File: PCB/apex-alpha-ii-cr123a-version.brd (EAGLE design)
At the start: 13.1 x 74.7 mm, 31 parts, among them IC1 CC430F5135, Y1 26MHz

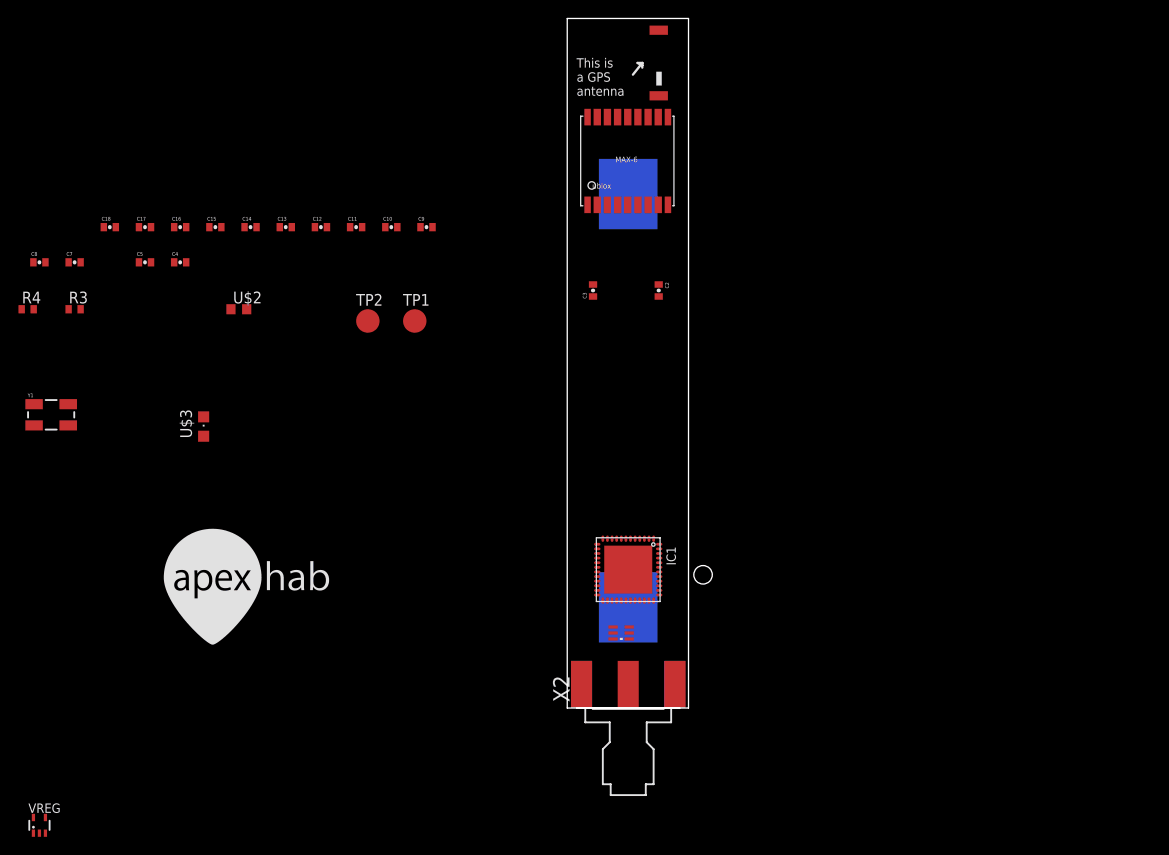
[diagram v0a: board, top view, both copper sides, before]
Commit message: Renamed to CR123a version
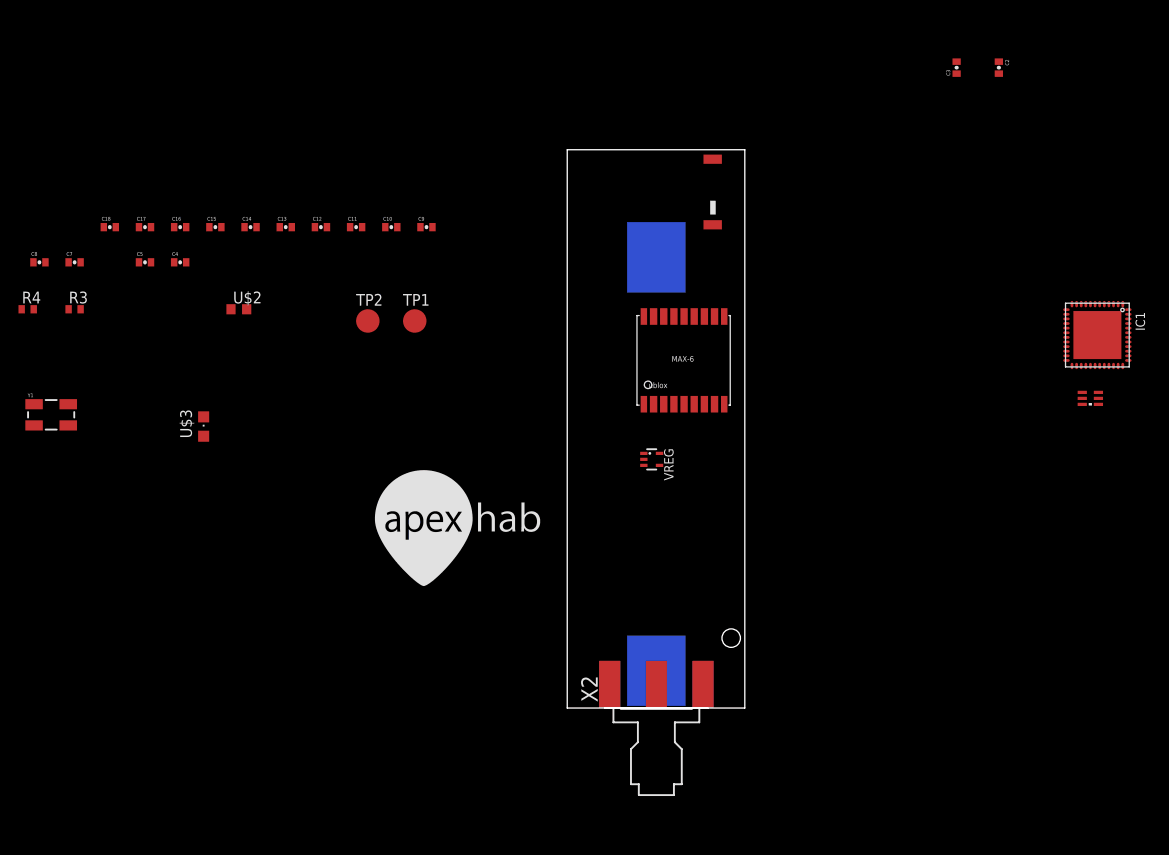
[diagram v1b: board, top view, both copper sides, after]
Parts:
- moved VREG 77.2 mm to (9.14, 26.9), turned to 270 degrees
- moved F1 56.8 mm to (56.6, 33.5)
- moved IC1 56.8 mm to (57.4, 40.4)
- moved C3 46.2 mm to (42.2, 69.3)
- moved C2 44.0 mm to (46.7, 69.3)
- moved JP1 23.7 mm to (-20.8, 13.2)
- moved GPS 22.4 mm to (12.7, 37.8)
- moved U$1 15.1 mm to (14.5, 56.1)
- moved CR123A 7.50 mm to (9.65, 26.4)
- moved X2 3.05 mm to (9.65, 0.00)
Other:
- board size 13.1 x 74.7 mm -> 19.2 x 60.5 mm
- board text removed: "This is a GPS antenna"
